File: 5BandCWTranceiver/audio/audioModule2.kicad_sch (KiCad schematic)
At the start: 59 parts, among them Q1 MMBT3906, Q2 MMBT3904, Q3 PZT2222A, Q4 PZT2907A

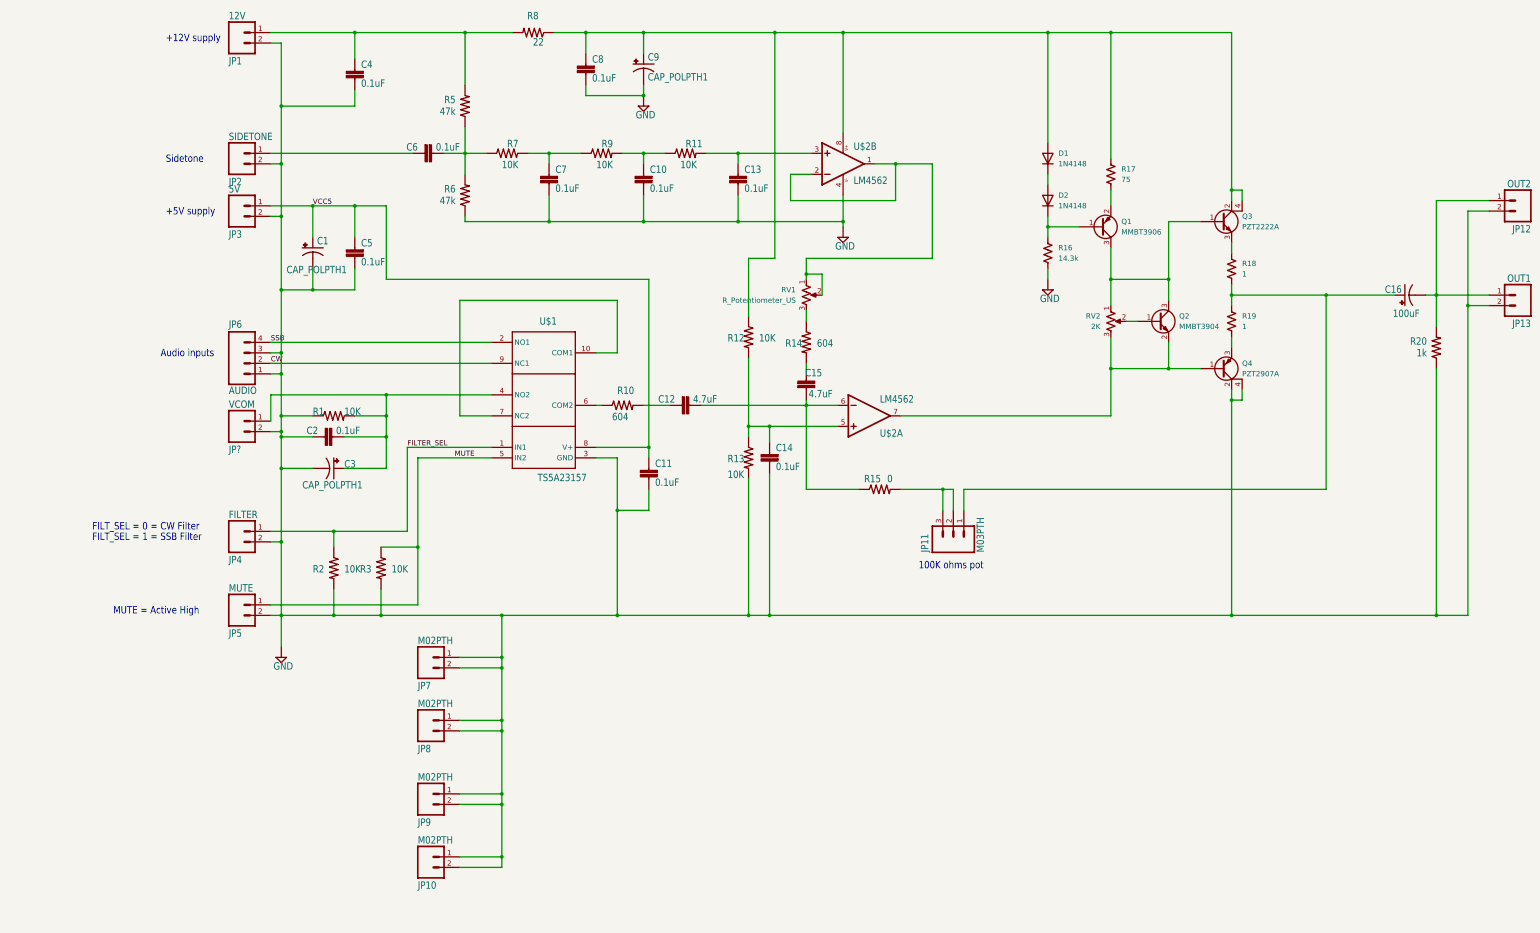
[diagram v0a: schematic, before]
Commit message: Update Audio Board
modify design and layout improvements
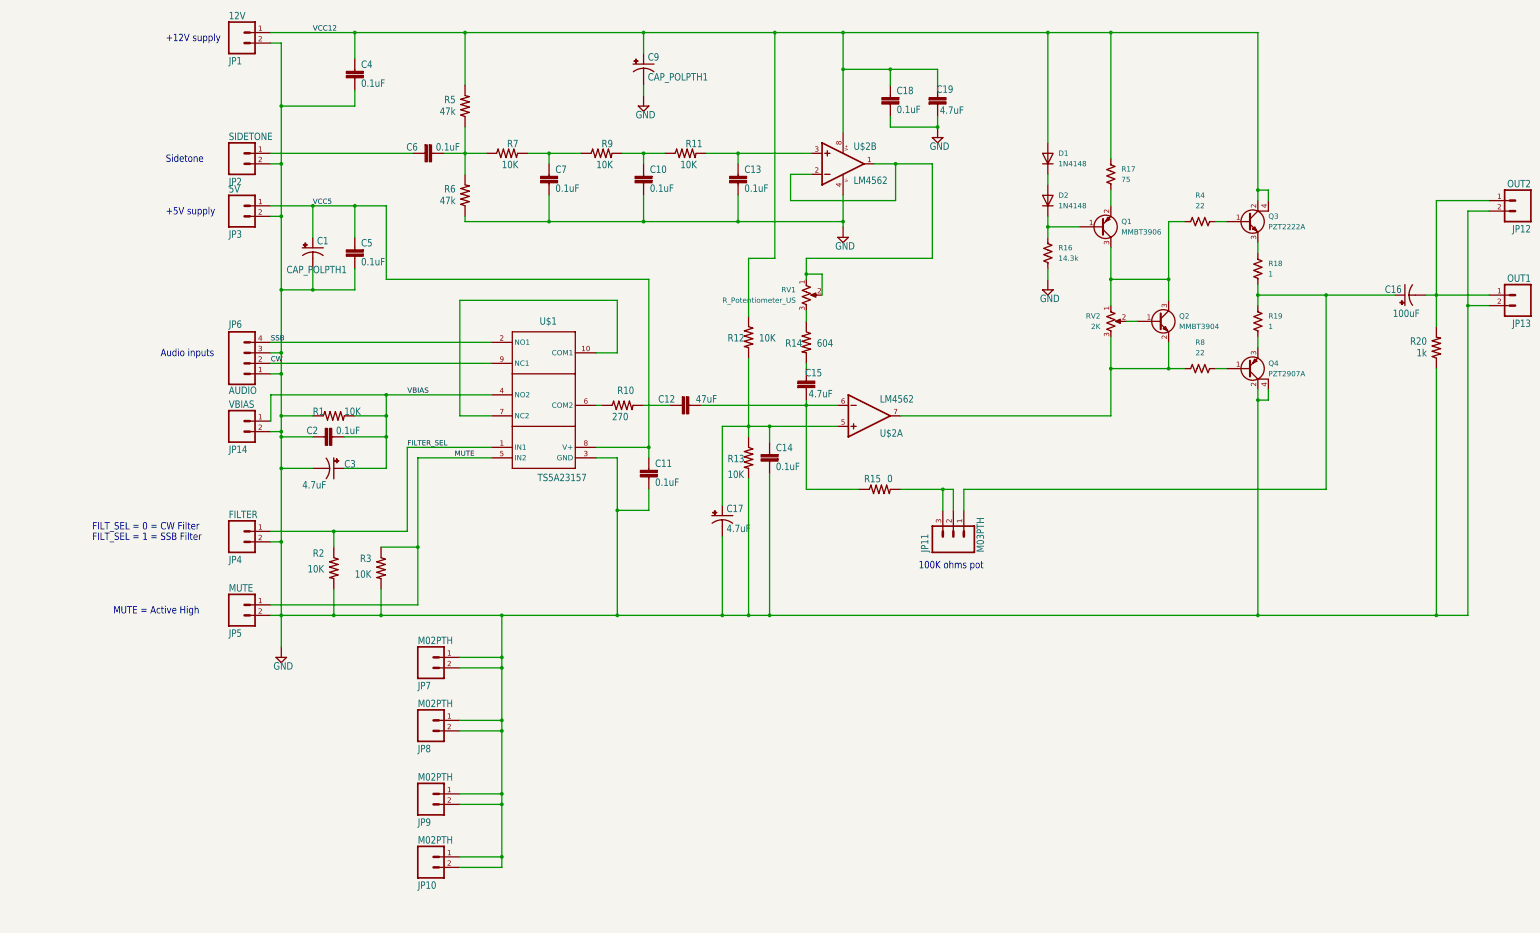
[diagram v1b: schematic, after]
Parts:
- removed C8: 0.1uF, Capacitor_SMD:C_0603_1608Metric_Pad1.08x0.95mm_HandSolder, symbol audioModule2-eagle-import:CAP0603-CAP
- removed R8: 22, Resistor_SMD:R_0603_1608Metric_Pad0.98x0.95mm_HandSolder, symbol audioModule2-eagle-import:RESISTOR0603-RES
- added C17: 4.7uF, Capacitor_THT:CP_Radial_D6.3mm_P2.50mm, symbol audioModule2-eagle-import:CAP_POLPTH1
- added C18: 0.1uF, Capacitor_SMD:C_0603_1608Metric_Pad1.08x0.95mm_HandSolder, symbol audioModule2-eagle-import:CAP0603-CAP
- added C19: 4.7uF, Capacitor_SMD:C_0603_1608Metric_Pad1.08x0.95mm_HandSolder, symbol audioModule2-eagle-import:CAP0603-CAP
- added R4, R8: 22, Resistor_SMD:R_0805_2012Metric_Pad1.20x1.40mm_HandSolder, symbol Device:R_US
- C12: value 4.7uF -> 47uF
- C3: value CAP_POLPTH1 -> 4.7uF
- JP14: renamed from JP?; value VCOM -> VBIAS
- R10: value 604 -> 270
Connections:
- net GND: now also C17.2 (-), C18.1, C19.2
- net VCC12: now reaches C9.1 (+), D1.2 (A), Q3.2 (C), Q3.4 (C), R12.1, R17.1, U$2.8 (V+)
- net VCC12: now also C4.2, JP1.1, R5.2, C18.2, C19.1
- net VBIAS: now reaches C2.1, C3.1 (+), JP14.1, R1.2, U$1.4 (NO2)
- net at Q1.3 (C), Q2.3 (C), RV2.1: now also R4.1; no longer Q3.1 (B)
- net at C14.2, R12.2, R13.1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: now also C17.1 (+)
- net at Q2.2 (E), RV2.3, U$2.7 (OUT): now also R8.1; no longer Q4.1 (B)
- new net: Q3.1 (B), R4.2
- new net: Q4.1 (B), R8.2
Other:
- moved on the sheet: Q3, Q4, R18, R19

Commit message: Tapeout - audio and power boards
Last mods to audio board; new power board
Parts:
- removed C12: 47uF, Capacitor_SMD:C_0603_1608Metric_Pad1.08x0.95mm_HandSolder, symbol audioModule2-eagle-import:CAP0603-CAP
- removed RV1: R_Potentiometer_US, Potentiometer_THT:Potentiometer_Bourns_3296W_Vertical, symbol Device:R_Potentiometer_US
- added C12, C8: 4.7uF, Capacitor_THT:CP_Radial_D6.3mm_P2.50mm, symbol audioModule2-eagle-import:CAP_POLPTH1
- R4, R8: value 22 -> 47
- U$2: value LM4562 -> OPA1678
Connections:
- net at R14.1: now also U$2.1 (OUT), U$2.2 (-IN)
- net at Q1.3 (C), Q2.3 (C), R4.1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: now also C12.1 (+)
- net at R10.2: now also C8.2 (-)
- net at Q2.2 (E), R8.1, RV2.3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: now also C12.2 (-)
- net at C15.2, R15.1, U$2.6 (-IN): now also C8.1 (+)
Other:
- moved on the sheet: C1, C10, C11, C13, C14, C15, C16, C17, C18, C19, C2, C3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

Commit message: Resync to Windows10
Getting synced to github with Windows10 laptop
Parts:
- C8: value 4.7uF -> 47uF
- R14: value 604 -> 11K
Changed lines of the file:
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@@
       (effects (font (size 1.778 1.5113)) (justify left bottom))
     )
-    (property "Value" "604" (id 1) (at 213.36 106.68 90)
+    (property "Value" "11K" (id 1) (at 213.36 106.68 90)
       (effects (font (size 1.778 1.5113)) (justify left bottom))
     )
@@
       (effects (font (size 1.778 1.5113)) (justify left bottom))
     )
-    (property "Value" "4.7uF" (id 1) (at 179.07 133.35 90)
+    (property "Value" "47uF" (id 1) (at 179.07 133.35 90)
       (effects (font (size 1.778 1.5113)) (justify left bottom))
     )
@@
     )
     (path "/2dabde6a-e117-4ebe-a2c4-fdfad659f488"
-      (reference "C8") (unit 1) (value "4.7uF") (footprint "Capacitor_THT:CP_Radial_D6.3mm_P2.50mm")
+      (reference "C8") (unit 1) (value "47uF") (footprint "Capacitor_THT:CP_Radial_D6.3mm_P2.50mm")
     )
     (path "/0747bbd6-9f56-4e24-bb75-d67f9e506c16"
@@
     )
     (path "/23101c8c-519d-4170-a1e1-a0d1c385ffb8"
-      (reference "R14") (unit 1) (value "604") (footprint "Resistor_SMD:R_0603_1608Metric_Pad0.98x0.95mm_HandSolder")
+      (reference "R14") (unit 1) (value "11K") (footprint "Resistor_SMD:R_0603_1608Metric_Pad0.98x0.95mm_HandSolder")
     )
     (path "/7f251369-eace-44ab-848c-cd3c5957381c"
